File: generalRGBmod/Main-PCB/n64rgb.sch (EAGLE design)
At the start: 74 parts, among them J1 MY_JUMPER, U1 5M570ZT100C5, U2 THS7374, U3 TLV70018-DDC

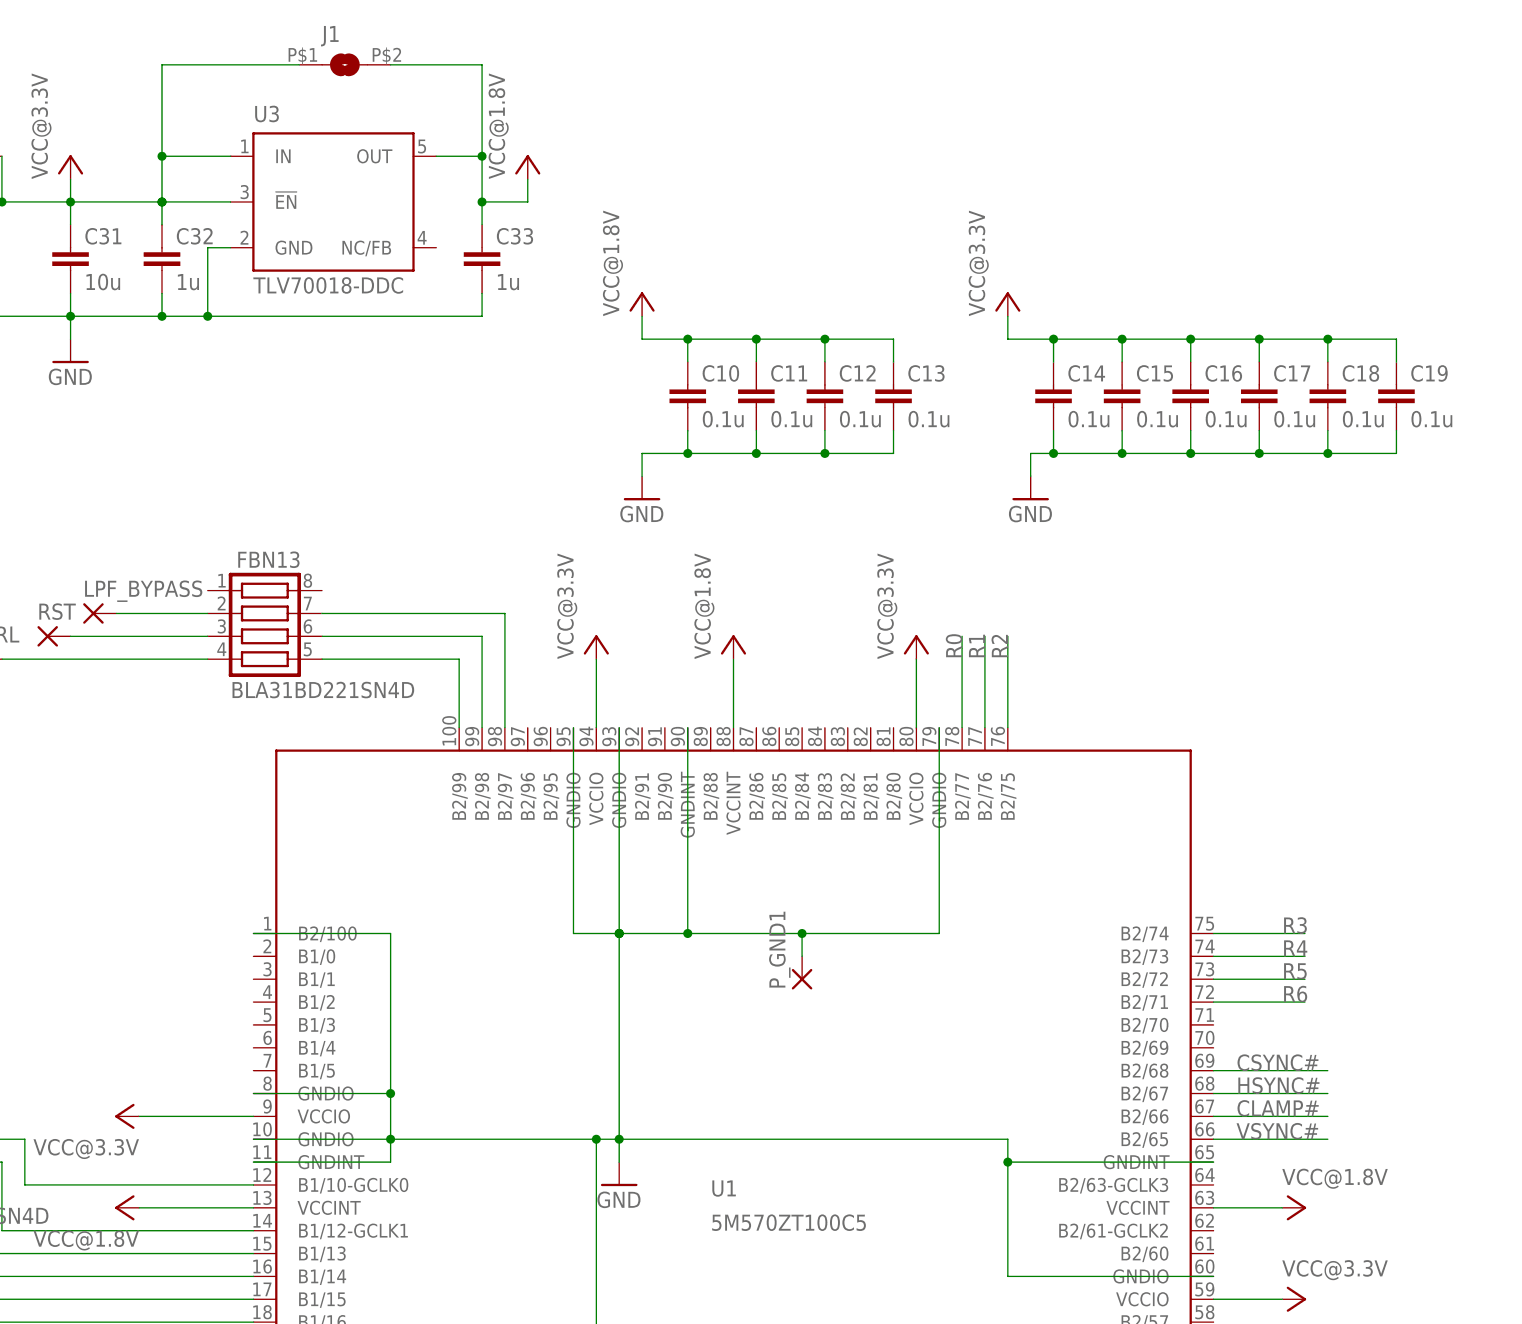
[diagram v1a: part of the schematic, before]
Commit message: Selectable installation type: either IGR or Switches
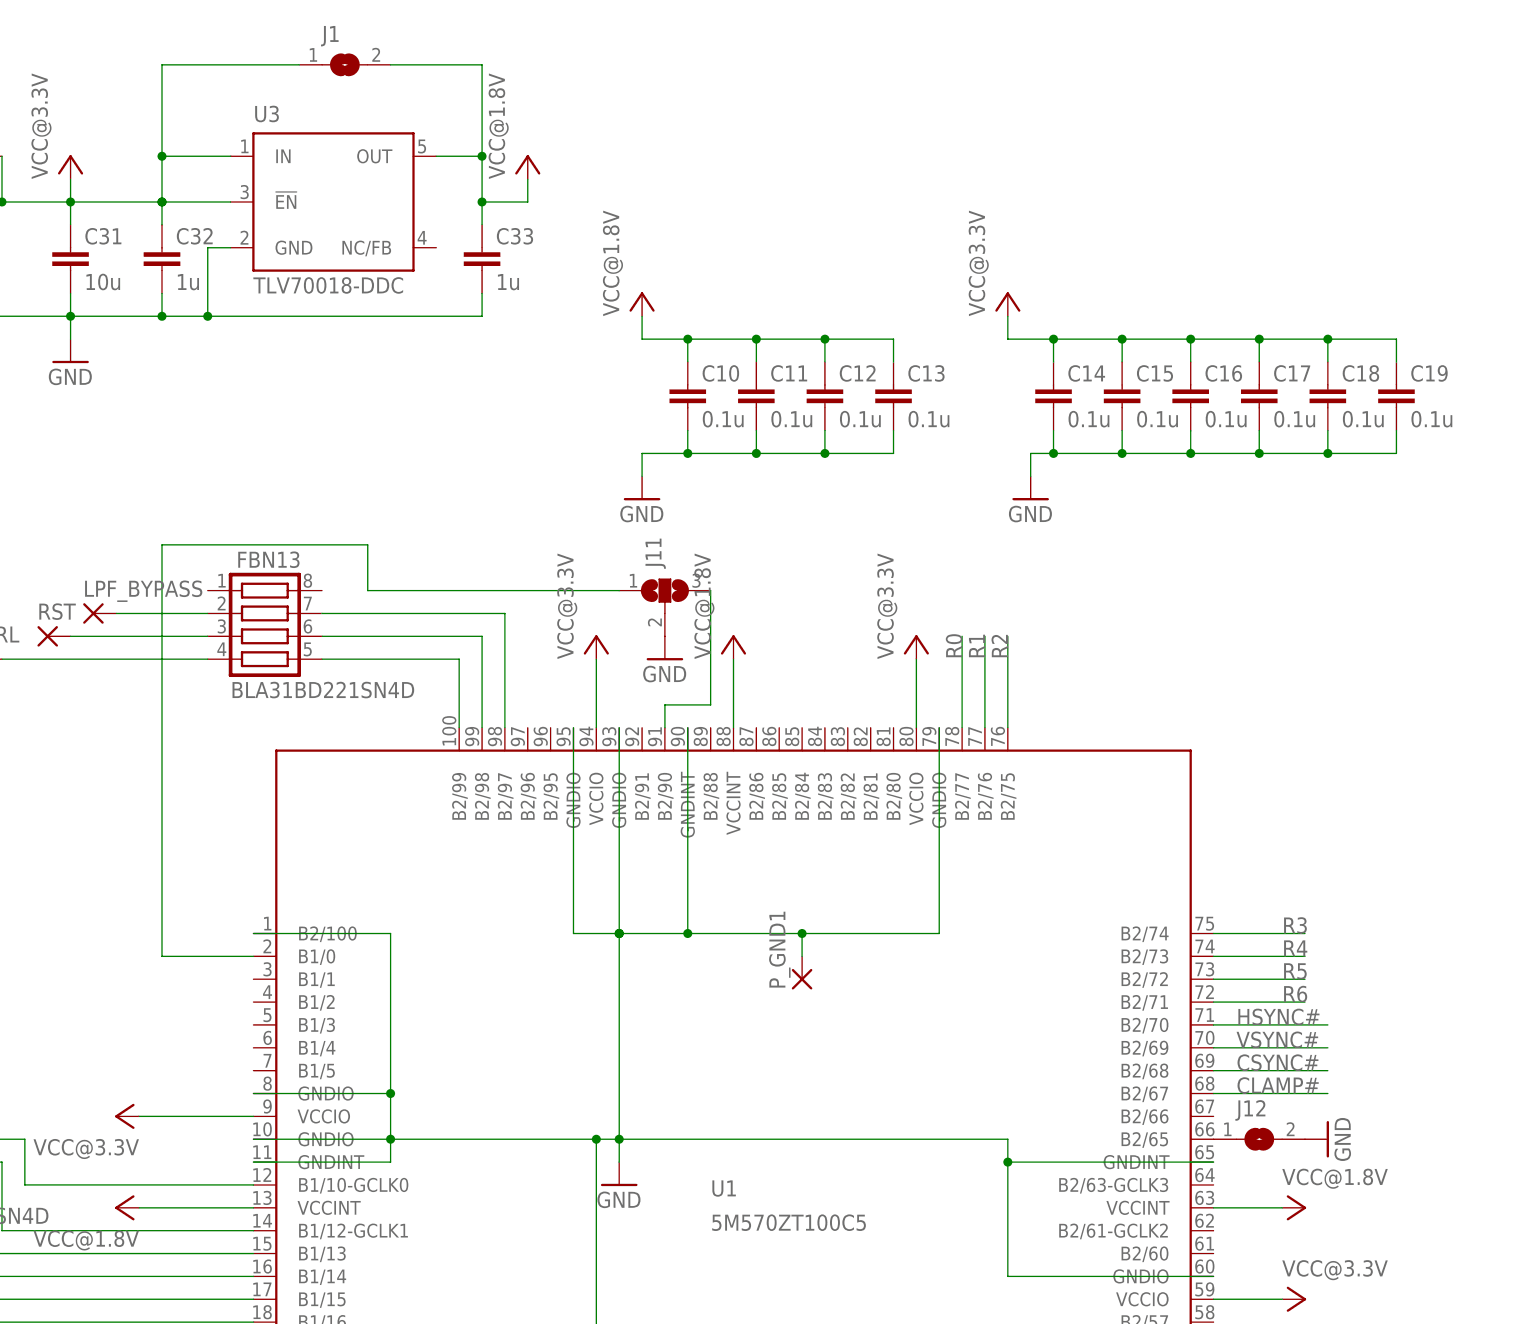
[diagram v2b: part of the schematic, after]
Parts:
- added J11: (no value), jumper:SJ2W
- added J12: (no value), jumper:SJ
- J1: value MY_JUMPER -> (none); device snes_div:MY_JUMPER -> jumper:SJ
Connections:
- new net N$49: J12.1, U1.B2/65
- new net N$51: J11.3, U1.B2/90
- new net N$52: J11.1, U1.B1/0
- net CLAMP#: now also U1.B2/67; no longer U1.B2/66
- net GND: now also J11.2, J12.2
- net HSYNC#: now also U1.B2/70; no longer U1.B2/67
- net VSYNC#: now also U1.B2/69; no longer U1.B2/65
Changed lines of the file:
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@@
 <?xml version="1.0" encoding="utf-8"?>
 <!DOCTYPE eagle SYSTEM "eagle.dtd">
-<eagle version="8.2.1">
+<eagle version="7.7.0">
 <drawing>
 <settings>
@@
 <part name="GND12" library="supply1" deviceset="GND" device=""/>
 <part name="FBN13" library="resistor-net" deviceset="CTS742C083" device="" value="BLA31BD221SN4D "/>
-<part name="J1" library="snes_div" deviceset="MY_JUMPER" device="" value=""/>
 <part name="R10" library="rcl" deviceset="R-EU_" device="R0603" value="1k"/>
 <part name="R11" library="rcl" deviceset="R-EU_" device="R0603" value="10k"/>
@@
 <part name="P+18" library="supply1" deviceset="VCC" device="" value="VCC@3.3V"/>
 <part name="GND3" library="supply1" deviceset="GND" device=""/>
+<part name="J12" library="jumper" deviceset="SJ" device=""/>
+<part name="J11" library="jumper" deviceset="SJ2W" device=""/>
+<part name="GND13" library="supply1" deviceset="GND" device=""/>
+<part name="GND18" library="supply1" deviceset="GND" device=""/>
+<part name="J1" library="jumper" deviceset="SJ" device=""/>
 </parts>
 <sheets>
@@
 <instance part="GND12" gate="1" x="76.2" y="63.5"/>
 <instance part="FBN13" gate="G$1" x="91.44" y="187.96"/>
-<instance part="J1" gate="G$1" x="101.6" y="248.92"/>
 <instance part="R10" gate="G$1" x="60.96" y="78.74" rot="R90"/>
 <instance part="R11" gate="G$1" x="53.34" y="78.74" rot="R90"/>
@@
 <instance part="P+18" gate="VCC" x="45.72" y="68.58" rot="R180"/>
 <instance part="GND3" gate="1" x="60.96" y="68.58"/>
+<instance part="J12" gate="1" x="203.2" y="129.54"/>
+<instance part="J11" gate="G$1" x="137.16" y="190.5" rot="R90"/>
+<instance part="GND13" gate="1" x="210.82" y="129.54" rot="R90"/>
+<instance part="GND18" gate="1" x="137.16" y="182.88"/>
+<instance part="J1" gate="1" x="101.6" y="248.92"/>
 </instances>
 <busses>
@@
 <wire x1="60.96" y1="71.12" x2="60.96" y2="73.66" width="0.1524" layer="91"/>
 </segment>
+<segment>
+<pinref part="J12" gate="1" pin="2"/>
+<pinref part="GND13" gate="1" pin="GND"/>
+</segment>
+<segment>
+<pinref part="J11" gate="G$1" pin="2"/>
+<pinref part="GND18" gate="1" pin="GND"/>
+</segment>
 </net>
 <net name="VCC@3.3V" class="0">
@@
 <wire x1="81.28" y1="238.76" x2="81.28" y2="248.92" width="0.1524" layer="91"/>
 <junction x="81.28" y="238.76"/>
-<pinref part="J1" gate="G$1" pin="1"/>
 <wire x1="81.28" y1="248.92" x2="96.52" y2="248.92" width="0.1524" layer="91"/>
+<pinref part="J1" gate="1" pin="1"/>
 </segment>
 <segment>
@@
 <net name="HSYNC#" class="0">
 <segment>
+<wire x1="198.12" y1="142.24" x2="210.82" y2="142.24" width="0.1524" layer="91"/>
+<pinref part="U1" gate="G$1" pin="B2/70"/>
+<label x="200.66" y="142.24" size="1.778" layer="95"/>
+</segment>
+</net>
+<net name="CLAMP#" class="0">
+<segment>
 <wire x1="198.12" y1="134.62" x2="210.82" y2="134.62" width="0.1524" layer="91"/>
 <label x="200.66" y="134.62" size="1.778" layer="95"/>
@@
 </segment>
 </net>
-<net name="CLAMP#" class="0">
-<segment>
-<wire x1="198.12" y1="132.08" x2="210.82" y2="132.08" width="0.1524" layer="91"/>
-<label x="200.66" y="132.08" size="1.778" layer="95"/>
-<pinref part="U1" gate="G$1" pin="B2/66"/>
-</segment>
-</net>
 <net name="VSYNC#" class="0">
 <segment>
-<wire x1="198.12" y1="129.54" x2="210.82" y2="129.54" width="0.1524" layer="91"/>
-<label x="200.66" y="129.54" size="1.778" layer="95"/>
-<pinref part="U1" gate="G$1" pin="B2/65"/>
+<wire x1="198.12" y1="139.7" x2="210.82" y2="139.7" width="0.1524" layer="91"/>
+<pinref part="U1" gate="G$1" pin="B2/69"/>
+<label x="200.66" y="139.7" size="1.778" layer="95"/>
 </segment>
 </net>
@@
 <wire x1="111.76" y1="238.76" x2="116.84" y2="238.76" width="0.1524" layer="91"/>
 <wire x1="116.84" y1="238.76" x2="116.84" y2="233.68" width="0.1524" layer="91"/>
-<pinref part="J1" gate="G$1" pin="2"/>
 <wire x1="106.68" y1="248.92" x2="116.84" y2="248.92" width="0.1524" layer="91"/>
 <wire x1="116.84" y1="248.92" x2="116.84" y2="238.76" width="0.1524" layer="91"/>
 <junction x="116.84" y="238.76"/>
+<pinref part="J1" gate="1" pin="2"/>
 </segment>
 <segment>
@@
 </segment>
 </net>
+<net name="N$49" class="0">
+<segment>
+<pinref part="U1" gate="G$1" pin="B2/65"/>
+<pinref part="J12" gate="1" pin="1"/>
+</segment>
+</net>
+<net name="N$51" class="0">
+<segment>
+<pinref part="U1" gate="G$1" pin="B2/90"/>
+<wire x1="137.16" y1="175.26" x2="137.16" y2="177.8" width="0.1524" layer="91"/>
+<pinref part="J11" gate="G$1" pin="3"/>
+<wire x1="137.16" y1="177.8" x2="142.24" y2="177.8" width="0.1524" layer="91"/>
+<wire x1="142.24" y1="177.8" x2="142.24" y2="190.5" width="0.1524" layer="91"/>
+</segment>
+</net>
+<net name="N$52" class="0">
+<segment>
+<pinref part="J11" gate="G$1" pin="1"/>
+<wire x1="132.08" y1="190.5" x2="104.14" y2="190.5" width="0.1524" layer="91"/>
+<wire x1="104.14" y1="190.5" x2="104.14" y2="195.58" width="0.1524" layer="91"/>
+<wire x1="104.14" y1="195.58" x2="81.28" y2="195.58" width="0.1524" layer="91"/>
+<wire x1="81.28" y1="195.58" x2="81.28" y2="149.86" width="0.1524" layer="91"/>
+<pinref part="U1" gate="G$1" pin="B1/0"/>
+<wire x1="81.28" y1="149.86" x2="91.44" y2="149.86" width="0.1524" layer="91"/>
+</segment>
+</net>

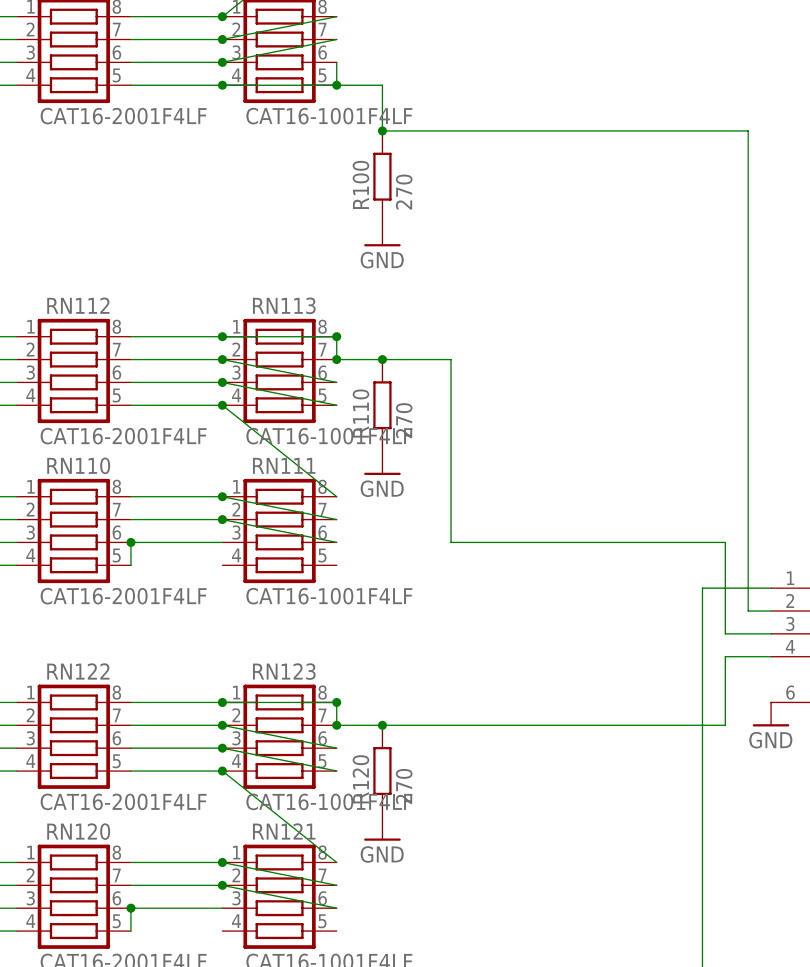
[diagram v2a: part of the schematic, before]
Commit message: change load resistor values at R2R output to have a more colourful picture
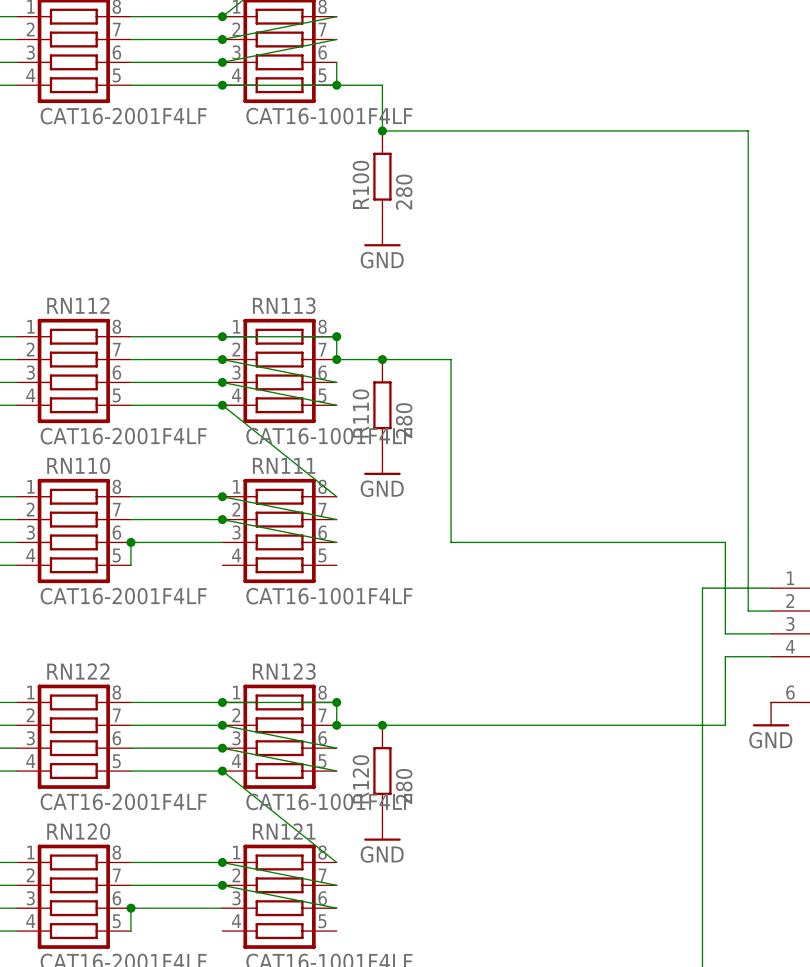
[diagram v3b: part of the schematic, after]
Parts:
- R100, R110, R120: value 270 -> 280
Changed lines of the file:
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@@
 <?xml version="1.0" encoding="utf-8"?>
 <!DOCTYPE eagle SYSTEM "eagle.dtd">
-<eagle version="7.7.0">
+<eagle version="8.4.3">
 <drawing>
 <settings>
 <setting alwaysvectorfont="no"/>
+<setting keepoldvectorfont="yes"/>
 <setting verticaltext="up"/>
 </settings>
@@
 <part name="RN101" library="resistor-net" deviceset="CTS742C083" device="" value="CAT16-1001F4LF "/>
 <part name="RN103" library="resistor-net" deviceset="CTS742C083" device="" value="CAT16-1001F4LF "/>
-<part name="R100" library="rcl" deviceset="R-EU_" device="R0603" value="270"/>
+<part name="R100" library="rcl" deviceset="R-EU_" device="R0603" value="280"/>
 <part name="GND22" library="supply1" deviceset="GND" device=""/>
 <part name="RN20" library="resistor-net" deviceset="CTS742C083" device="" value="CAT16-75R0F4LF "/>
@@
 <part name="RN111" library="resistor-net" deviceset="CTS742C083" device="" value="CAT16-1001F4LF "/>
 <part name="RN113" library="resistor-net" deviceset="CTS742C083" device="" value="CAT16-1001F4LF "/>
-<part name="R110" library="rcl" deviceset="R-EU_" device="R0603" value="270"/>
+<part name="R110" library="rcl" deviceset="R-EU_" device="R0603" value="280"/>
 <part name="GND9" library="supply1" deviceset="GND" device=""/>
 <part name="RN120" library="resistor-net" deviceset="CTS742C083" device="" value="CAT16-2001F4LF "/>
@@
 <part name="RN121" library="resistor-net" deviceset="CTS742C083" device="" value="CAT16-1001F4LF "/>
 <part name="RN123" library="resistor-net" deviceset="CTS742C083" device="" value="CAT16-1001F4LF "/>
-<part name="R120" library="rcl" deviceset="R-EU_" device="R0603" value="270"/>
+<part name="R120" library="rcl" deviceset="R-EU_" device="R0603" value="280"/>
 <part name="GND10" library="supply1" deviceset="GND" device=""/>
 <part name="DSYNC#" library="wirepad" deviceset="SMD1" device="" value=""/>

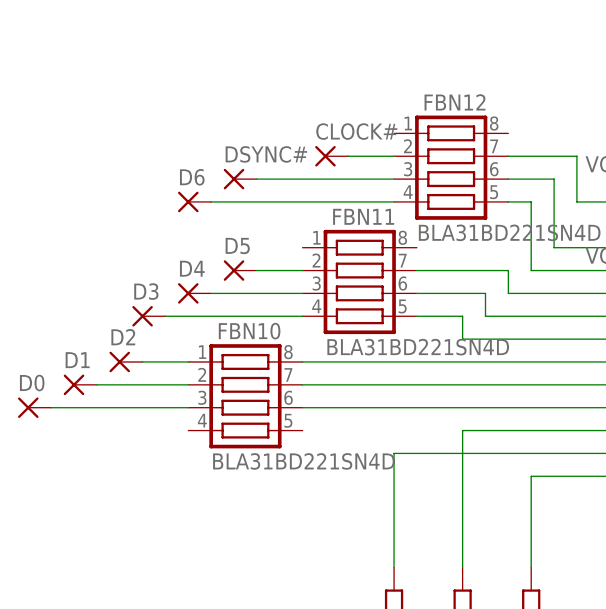
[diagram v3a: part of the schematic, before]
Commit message: Update PCB: add logo, new name, stencil reduce pad size by 10%
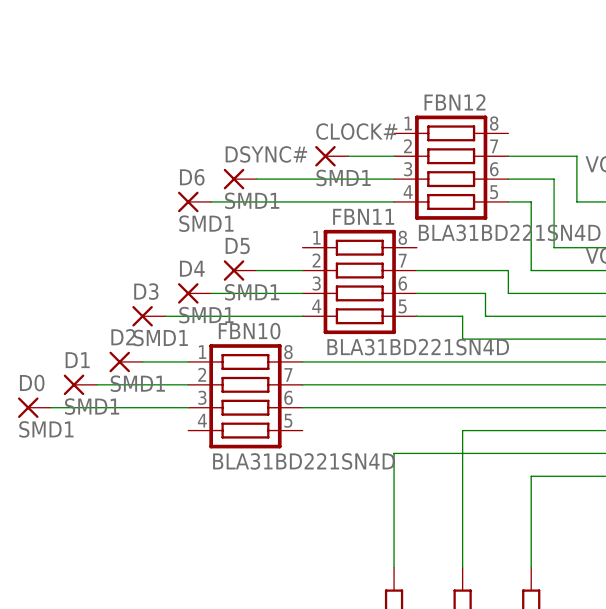
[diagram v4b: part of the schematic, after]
